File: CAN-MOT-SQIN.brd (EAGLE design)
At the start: 25.4 x 25.4 mm, 24 parts, among them U1 TLV760, U2 MCP25625ML, U3 BTM7752G, U4 ATTINY816M, Y1 16MHz

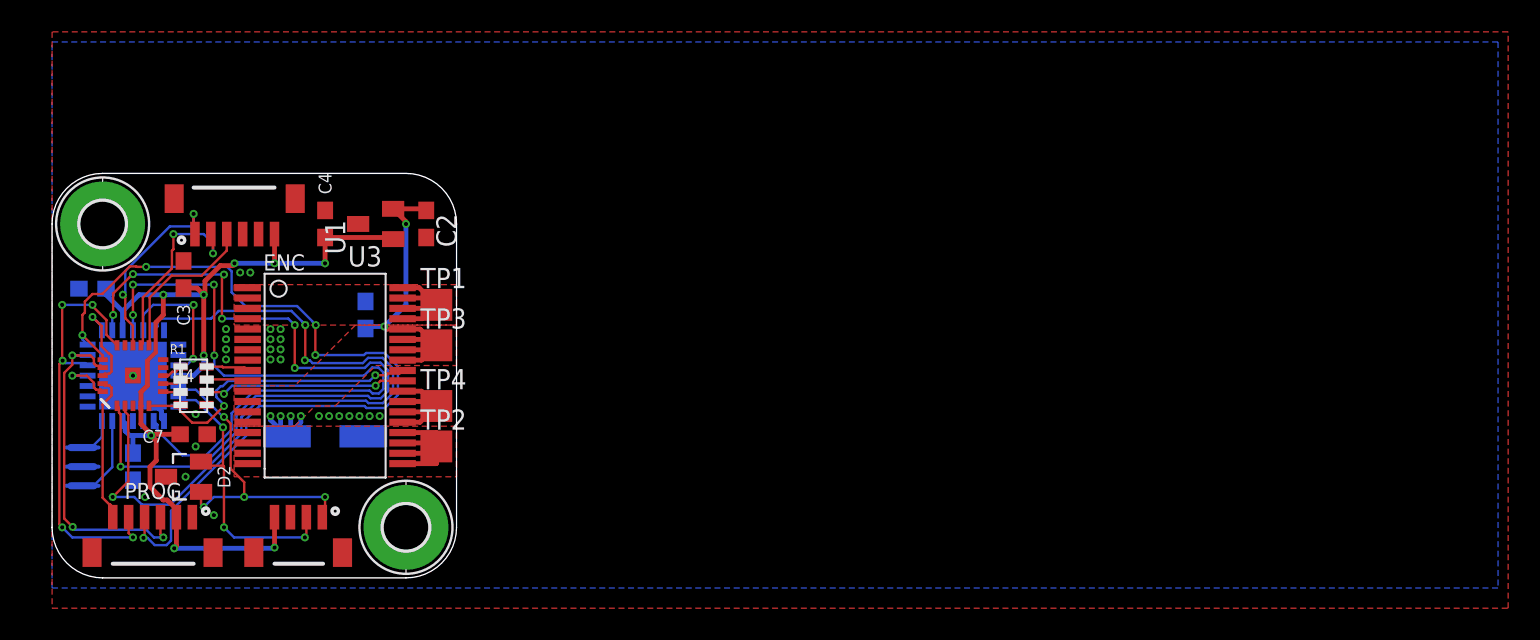
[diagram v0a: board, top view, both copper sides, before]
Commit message: Now with better silkscreen
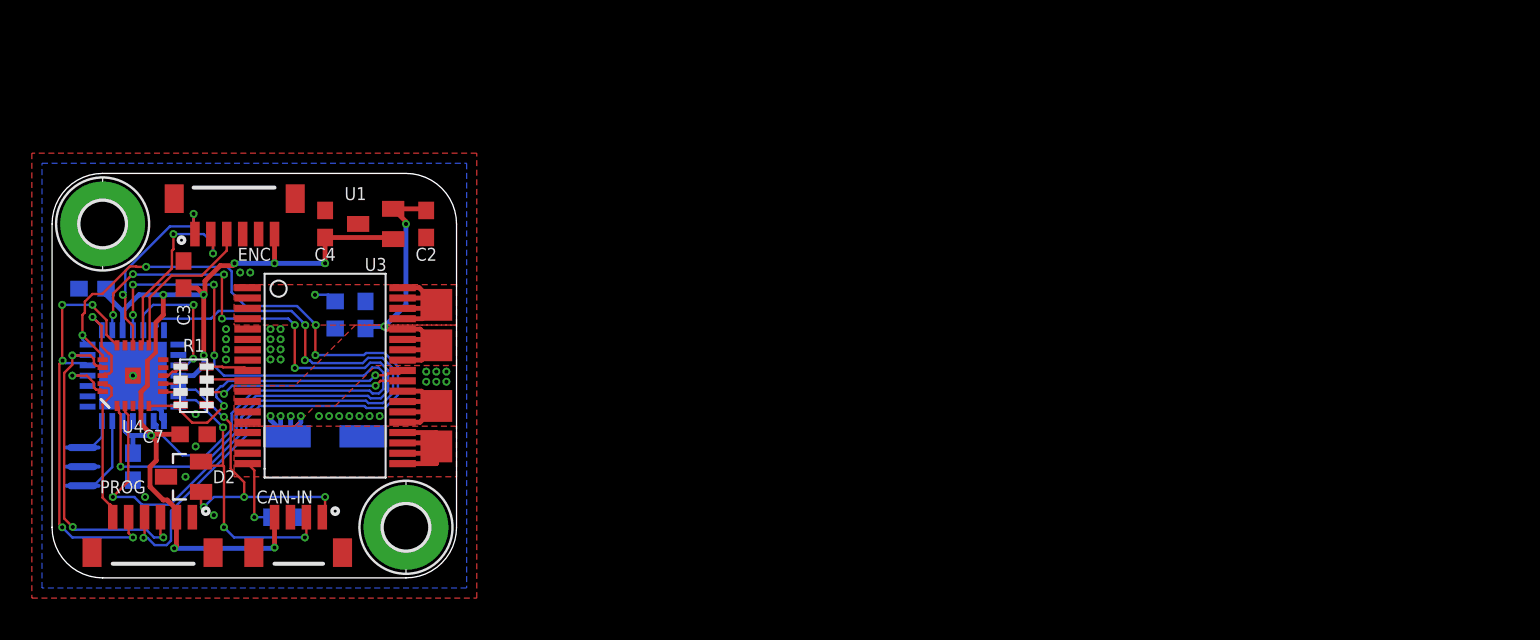
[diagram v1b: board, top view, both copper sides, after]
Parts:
- added R2, R3: 100K, resistor:R0603
- C6: value (none) -> 100u/35V
- R1: value (none) -> 1K
- renumbered TP1 to MOT1, TP2 to MOT2, TP3 to VS, TP4 to GND
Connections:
- net N$12 renamed IN2
- net N$13 renamed IN1
- net N$4 renamed CANH
- net N$5 renamed CANL
- net N$8 renamed IS
- net N$9 renamed INH
- net GND: now also R2.1, R3.1
- net MOT1: now also R2.2
- net MOT2: now also R3.2
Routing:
- net MOT2: track 10.6 -> 15.2 mm, vias 0 -> 1
- net MOT1: track 9.56 -> 11.0 mm, vias 0 -> 1
- net GND: vias 27 -> 33

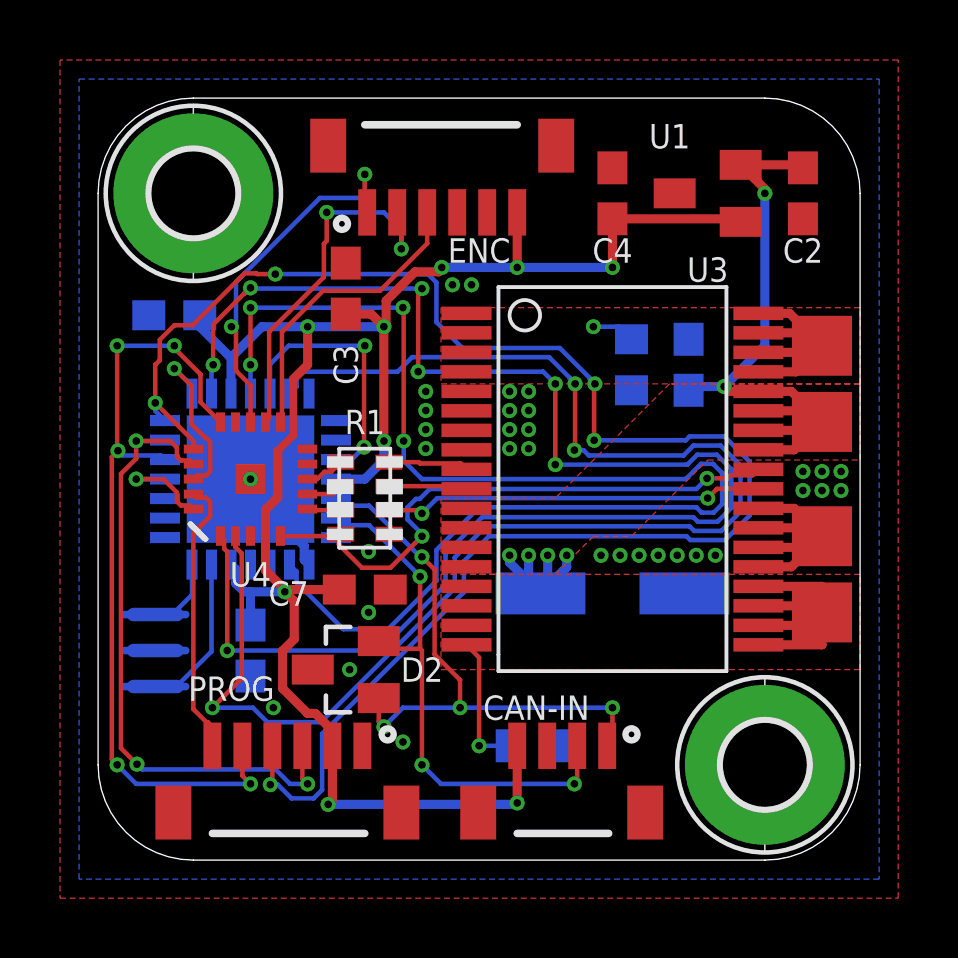
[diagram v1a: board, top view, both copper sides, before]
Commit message: Re-routed so now the peripherals will do the right thing
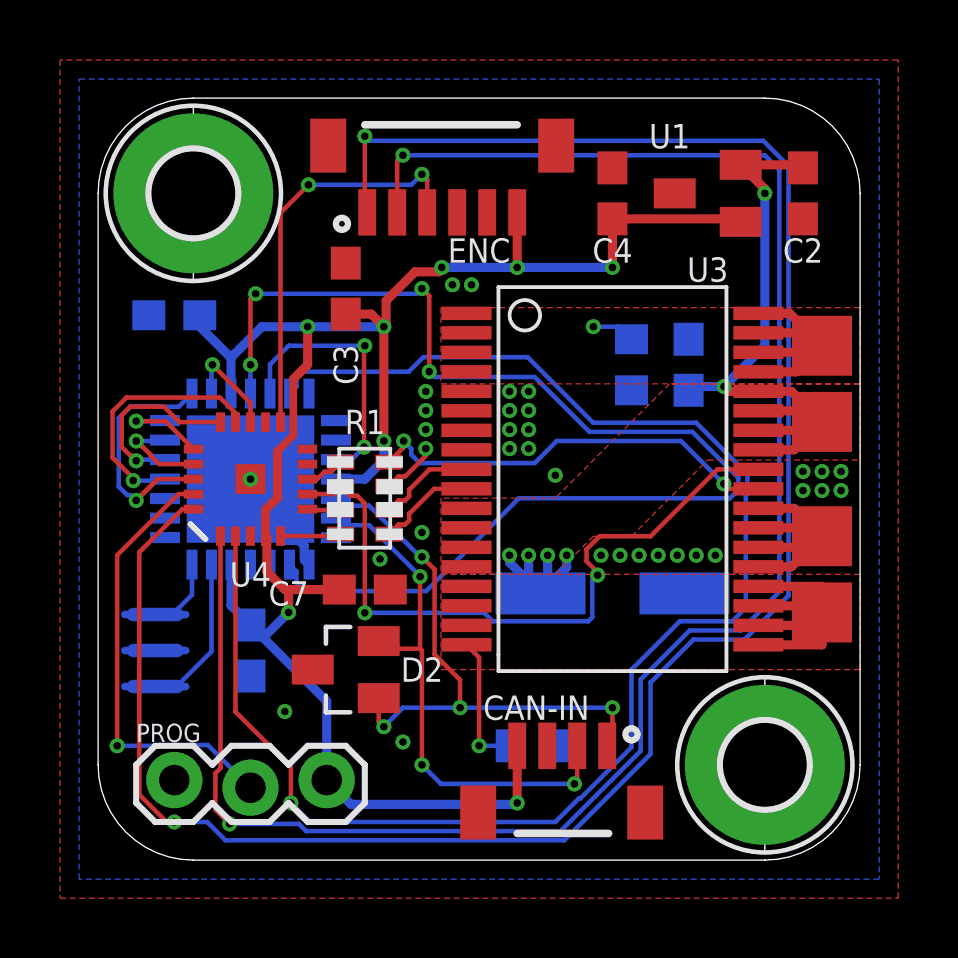
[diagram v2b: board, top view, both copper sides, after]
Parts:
- PROG: value STRAWSON_EAGLE_LIB_JST_SH_6 -> (none); device can-library:STRAWSON_EAGLE_LIB_JST_SH_6 -> SparkFun-Connectors:1X03_LOCK
- moved PROG 1.80 mm to (2.54, 2.54)
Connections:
- removed net RST: PROG.6, U4.19
- new net RST/UDPI: PROG.2, U4.19
- net +5V: now also PROG.3; no longer PROG.2
- net A: now also U4.20; no longer U4.13
- net B: now also U4.1; no longer U4.12
- net CAN_RESET: now also U4.13; no longer U4.1
- net GND: now also R1.4; no longer R1.8
- net IN1: now also R1.5, U4.6; no longer R1.1, U4.8
- net IN2: now also R1.7, U4.5; no longer R1.3, U4.7
- net INH: now also R1.1, U4.8; no longer R1.5, U4.6
- net INTERRUPT: now also U4.14; no longer U4.20
- net IS: now also R1.3, U4.7; no longer R1.7, U4.5
- net MISO: no longer PROG.4
- net MOSI: no longer PROG.3
- net N$3: now also R1.6; no longer R1.2
- net N$6: now also R1.8; no longer R1.4
- net N$7: now also R1.2; no longer R1.6
- net SCK: no longer PROG.5
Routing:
- net A: track 12.5 -> 69.0 mm
- net MISO: track 55.2 -> 3.26 mm, vias 5 -> 1
- net B: track 12.5 -> 61.8 mm
- net CAN_RESET: track 51.0 -> 3.41 mm, vias 7 -> 1
- net SCK: track 27.0 -> 6.33 mm, vias 5 -> 1
- net MOSI: track 21.9 -> 3.21 mm, vias 3 -> 1
- net RST/UDPI: track 0.00 -> 14.8 mm, vias 0 -> 1
- net RST: track 9.33 -> 0.00 mm
- net INTERRUPT: track 3.46 -> 8.47 mm
- net IS: track 19.2 -> 23.0 mm
- net CLK: track 48.0 -> 51.6 mm, vias 3 -> 1
- net Z: track 10.1 -> 13.6 mm, vias 0 -> 2
- net !CAN_CS!: track 5.68 -> 8.88 mm
- net N$1: track 43.3 -> 41.0 mm
- net GND: track 13.0 -> 14.9 mm
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
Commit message: Fixed the routing so now it will (probably) work as intended
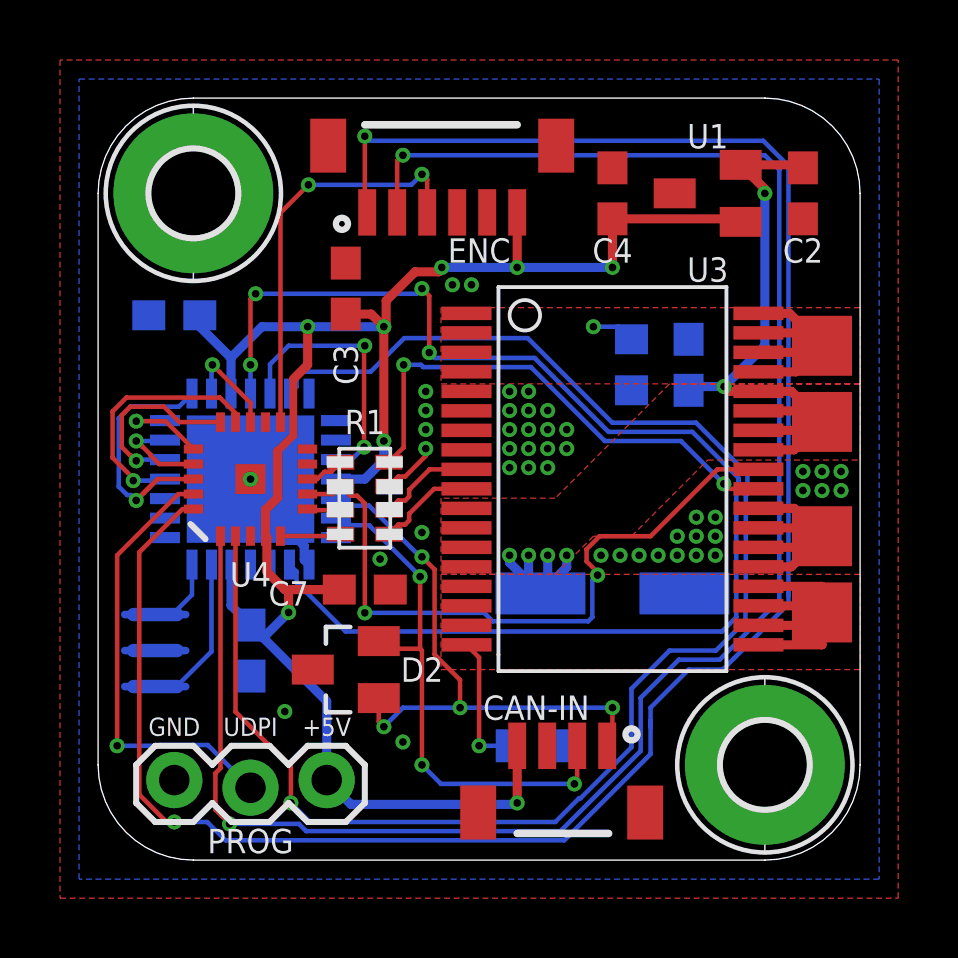
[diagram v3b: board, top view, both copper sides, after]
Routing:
- net N$1: track 41.0 -> 44.6 mm
- net N$7: track 14.1 -> 17.0 mm
- net GND: vias 33 -> 45
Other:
- board text added: "+5V"
- board text added: "GND"
- board text added: "UDPI"

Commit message: Revised with the correct ATTINY816 footprint and external logic for the encoder
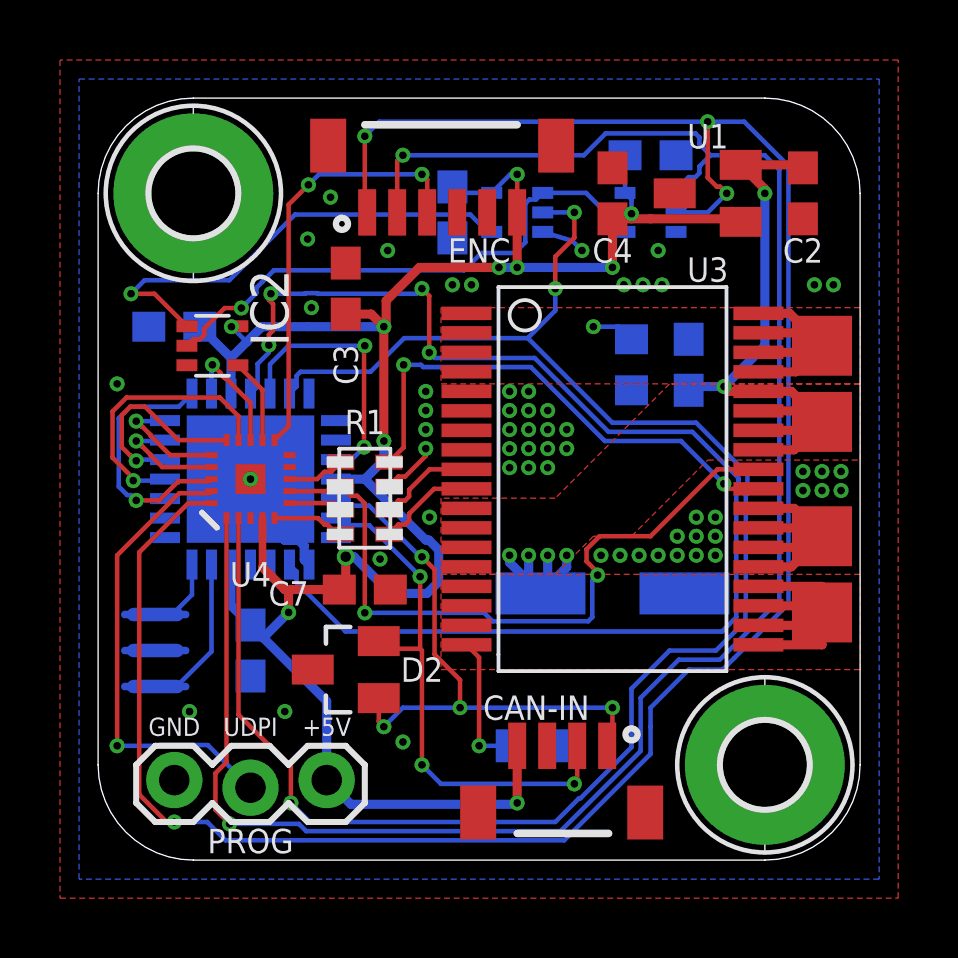
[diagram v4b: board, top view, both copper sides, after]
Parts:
- added C11, C9: 100n, resistor:C0603
- added IC1, IC2: 74AHC1G86DCK, 74xx-little-us:SC70-5
- added IC3: 74LVC1G79DCK, 74xx-little-us:SC70-5
- moved C1 0.38 mm to (2.54, 17.8)
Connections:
- new net N$4: IC2.1, IC3.4
- new net N$5: IC1.4, IC2.2, IC3.1
- new net N$8: IC2.4, U4.12
- net +5V: now also C11.1, C9.1, IC1.5, IC2.5, IC3.5
- net A: now also IC1.2
- net B: now also IC1.1
- net CLK: now also IC3.2
- net GND: now also C11.2, C9.2, IC1.3, IC2.3, IC3.3
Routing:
- net N$5: track 0.00 -> 18.2 mm, vias 0 -> 1
- net N$4: track 0.00 -> 15.7 mm, vias 0 -> 1
- net +5V: track 64.7 -> 74.3 mm, vias 8 -> 11
- net CLK: track 52.0 -> 58.5 mm, vias 1 -> 3
- net A: track 68.9 -> 74.4 mm, vias 2 -> 4
- net B: track 61.6 -> 64.9 mm
- net N$8: track 0.00 -> 2.83 mm
- net GND: track 14.9 -> 16.4 mm, vias 45 -> 58
- net MISO: track 3.26 -> 3.96 mm
- net IN1: track 1.12 -> 1.81 mm
- net Z: track 13.6 -> 14.2 mm
- net RST/UDPI: track 14.8 -> 15.4 mm
- net MOSI: track 3.21 -> 3.86 mm
- net INTERRUPT: track 8.47 -> 9.12 mm
- net CAN_RESET: track 3.41 -> 4.03 mm
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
